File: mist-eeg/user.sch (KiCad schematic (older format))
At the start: 18 parts, among them SW1 START, SW2 USER

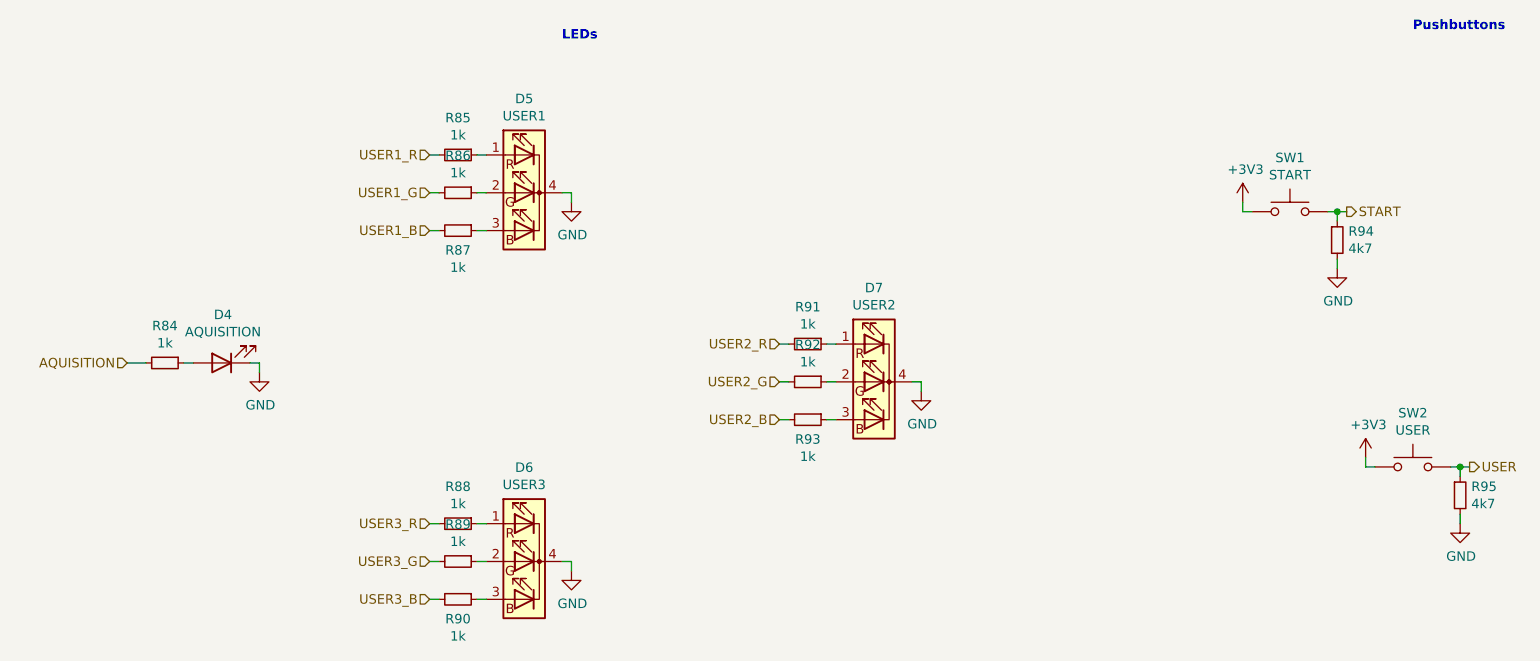
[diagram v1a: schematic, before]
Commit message: Finish schematic and create interface specifications
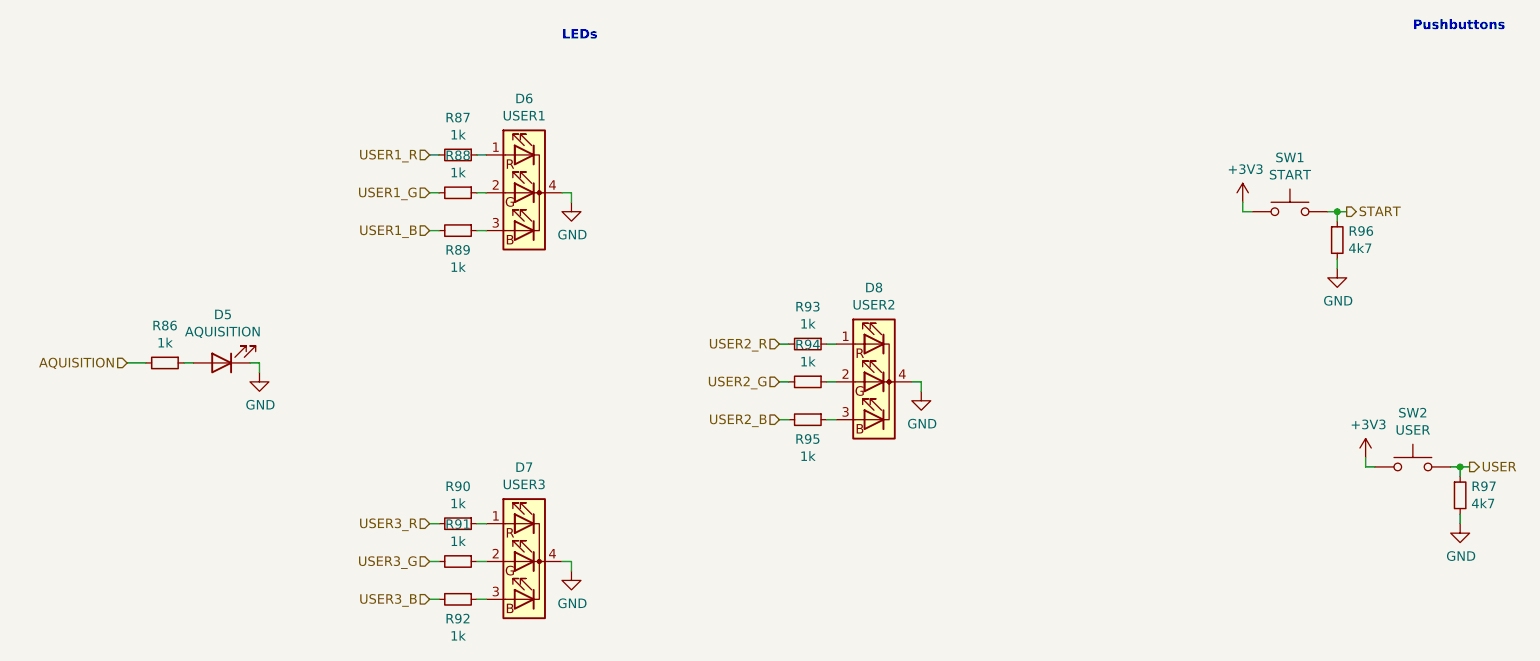
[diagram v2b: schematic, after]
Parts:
- renumbered D4 to D5, D5 to D6, D6 to D7, D7 to D8, R84 to R86, R85 to R87, R86 to R88, R87 to R89, R88 to R90, R89 to R91, R90 to R92, R91 to R93, R92 to R94, R93 to R95, R94 to R96, R95 to R97
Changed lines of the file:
@@
 $EndDescr
 $Comp
-L Device:LED_RGBC D5
+L Device:LED_RGBC D6
 U 1 1 60D2487F
 P 3500 3250
-F 0 "D5" H 3500 3747 50  0000 C CNN
+F 0 "D6" H 3500 3747 50  0000 C CNN
 F 1 "USER1" H 3500 3656 50  0000 C CNN
 F 2 "LED_THT:LED_D5.0mm-4_RGB" H 3500 3200 50  0001 C CNN
@@
 $EndComp
 $Comp
-L power:GND #PWR0108
+L power:GND #PWR0109
 U 1 1 60D255D9
 P 3750 3300
-F 0 "#PWR0108" H 3750 3050 50  0001 C CNN
+F 0 "#PWR0109" H 3750 3050 50  0001 C CNN
 F 1 "GND" H 3755 3127 50  0000 C CNN
 F 2 "" H 3750 3300 50  0001 C CNN
@@
 	3750 3250 3700 3250
 $Comp
-L Device:R_Small R85
+L Device:R_Small R87
 U 1 1 60D26A9C
 P 3150 3050
-F 0 "R85" V 2954 3050 50  0000 C CNN
+F 0 "R87" V 2954 3050 50  0000 C CNN
 F 1 "1k" V 3045 3050 50  0000 C CNN
 F 2 "Resistor_SMD:R_0402_1005Metric" H 3150 3050 50  0001 C CNN
@@
 	3000 3050 3050 3050
 $Comp
-L Device:R_Small R86
+L Device:R_Small R88
 U 1 1 60D27725
 P 3150 3250
-F 0 "R86" V 2954 3250 50  0000 C CNN
+F 0 "R88" V 2954 3250 50  0000 C CNN
 F 1 "1k" V 3045 3250 50  0000 C CNN
 F 2 "Resistor_SMD:R_0402_1005Metric" H 3150 3250 50  0001 C CNN
@@
 	3000 3250 3050 3250
 $Comp
-L Device:R_Small R87
+L Device:R_Small R89
 U 1 1 60D27A38
 P 3150 3450
-F 0 "R87" V 3254 3450 50  0000 C CNN
+F 0 "R89" V 3254 3450 50  0000 C CNN
 F 1 "1k" V 3345 3450 50  0000 C CNN
 F 2 "Resistor_SMD:R_0402_1005Metric" H 3150 3450 50  0001 C CNN
@@
 	3000 3450 3050 3450
 $Comp
-L Device:LED_RGBC D7
+L Device:LED_RGBC D8
 U 1 1 60D29FC0
 P 5350 4250
-F 0 "D7" H 5350 4747 50  0000 C CNN
+F 0 "D8" H 5350 4747 50  0000 C CNN
 F 1 "USER2" H 5350 4656 50  0000 C CNN
 F 2 "LED_THT:LED_D5.0mm-4_RGB" H 5350 4200 50  0001 C CNN
@@
 $EndComp
 $Comp
-L power:GND #PWR0110
+L power:GND #PWR0111
 U 1 1 60D29FC6
 P 5600 4300
-F 0 "#PWR0110" H 5600 4050 50  0001 C CNN
+F 0 "#PWR0111" H 5600 4050 50  0001 C CNN
 F 1 "GND" H 5605 4127 50  0000 C CNN
 F 2 "" H 5600 4300 50  0001 C CNN
@@
 	5600 4250 5550 4250
 $Comp
-L Device:R_Small R91
+L Device:R_Small R93
 U 1 1 60D29FCE
 P 5000 4050
-F 0 "R91" V 4804 4050 50  0000 C CNN
+F 0 "R93" V 4804 4050 50  0000 C CNN
 F 1 "1k" V 4895 4050 50  0000 C CNN
 F 2 "Resistor_SMD:R_0402_1005Metric" H 5000 4050 50  0001 C CNN
@@
 	4850 4050 4900 4050
 $Comp
-L Device:R_Small R92
+L Device:R_Small R94
 U 1 1 60D29FD7
 P 5000 4250
-F 0 "R92" V 4804 4250 50  0000 C CNN
+F 0 "R94" V 4804 4250 50  0000 C CNN
 F 1 "1k" V 4895 4250 50  0000 C CNN
 F 2 "Resistor_SMD:R_0402_1005Metric" H 5000 4250 50  0001 C CNN
@@
 	4850 4250 4900 4250
 $Comp
-L Device:R_Small R93
+L Device:R_Small R95
 U 1 1 60D29FE0
 P 5000 4450
-F 0 "R93" V 5104 4450 50  0000 C CNN
+F 0 "R95" V 5104 4450 50  0000 C CNN
 F 1 "1k" V 5195 4450 50  0000 C CNN
 F 2 "Resistor_SMD:R_0402_1005Metric" H 5000 4450 50  0001 C CNN
@@
 	4850 4450 4900 4450
 $Comp
-L Device:LED_RGBC D6
+L Device:LED_RGBC D7
 U 1 1 60D2CF7B
 P 3500 5200
-F 0 "D6" H 3500 5697 50  0000 C CNN
+F 0 "D7" H 3500 5697 50  0000 C CNN
 F 1 "USER3" H 3500 5606 50  0000 C CNN
 F 2 "LED_THT:LED_D5.0mm-4_RGB" H 3500 5150 50  0001 C CNN
@@
 $EndComp
 $Comp
-L power:GND #PWR0109
+L power:GND #PWR0110
 U 1 1 60D2CF81
 P 3750 5250
-F 0 "#PWR0109" H 3750 5000 50  0001 C CNN
+F 0 "#PWR0110" H 3750 5000 50  0001 C CNN
 F 1 "GND" H 3755 5077 50  0000 C CNN
 F 2 "" H 3750 5250 50  0001 C CNN
@@
 	3750 5200 3700 5200
 $Comp
-L Device:R_Small R88
+L Device:R_Small R90
 U 1 1 60D2CF89
 P 3150 5000
-F 0 "R88" V 2954 5000 50  0000 C CNN
+F 0 "R90" V 2954 5000 50  0000 C CNN
 F 1 "1k" V 3045 5000 50  0000 C CNN
 F 2 "Resistor_SMD:R_0402_1005Metric" H 3150 5000 50  0001 C CNN
@@
 	3000 5000 3050 5000
 $Comp
-L Device:R_Small R89
+L Device:R_Small R91
 U 1 1 60D2CF92
 P 3150 5200
-F 0 "R89" V 2954 5200 50  0000 C CNN
+F 0 "R91" V 2954 5200 50  0000 C CNN
 F 1 "1k" V 3045 5200 50  0000 C CNN
 F 2 "Resistor_SMD:R_0402_1005Metric" H 3150 5200 50  0001 C CNN
@@
 	3000 5200 3050 5200
 $Comp
-L Device:R_Small R90
+L Device:R_Small R92
 U 1 1 60D2CF9B
 P 3150 5400
-F 0 "R90" V 3254 5400 50  0000 C CNN
+F 0 "R92" V 3254 5400 50  0000 C CNN
 F 1 "1k" V 3345 5400 50  0000 C CNN
 F 2 "Resistor_SMD:R_0402_1005Metric" H 3150 5400 50  0001 C CNN
@@
 	7800 3650 7800 3600
 $Comp
-L power:GND #PWR0112
+L power:GND #PWR0113
 U 1 1 60D6D004
 P 7800 3650
-F 0 "#PWR0112" H 7800 3400 50  0001 C CNN
+F 0 "#PWR0113" H 7800 3400 50  0001 C CNN
 F 1 "GND" H 7805 3477 50  0000 C CNN
 F 2 "" H 7800 3650 50  0001 C CNN
@@
 $EndComp
 $Comp
-L Device:R_Small R94
+L Device:R_Small R96
 U 1 1 60D6CBEB
 P 7800 3500
-F 0 "R94" H 7859 3546 50  0000 L CNN
+F 0 "R96" H 7859 3546 50  0000 L CNN
 F 1 "4k7" H 7859 3455 50  0000 L CNN
 F 2 "Resistor_SMD:R_0201_0603Metric" H 7800 3500 50  0001 C CNN
@@
 	2100 4200 2100 4150
 $Comp
-L power:GND #PWR0107
+L power:GND #PWR0108
 U 1 1 60D1F73E
 P 2100 4200
-F 0 "#PWR0107" H 2100 3950 50  0001 C CNN
+F 0 "#PWR0108" H 2100 3950 50  0001 C CNN
 F 1 "GND" H 2105 4027 50  0000 C CNN
 F 2 "" H 2100 4200 50  0001 C CNN
@@
 	1700 4150 1750 4150
 $Comp
-L Device:R_Small R84
+L Device:R_Small R86
 U 1 1 60D1C4D3
 P 1600 4150
-F 0 "R84" V 1404 4150 50  0000 C CNN
+F 0 "R86" V 1404 4150 50  0000 C CNN
 F 1 "1k" V 1495 4150 50  0000 C CNN
 F 2 "Resistor_SMD:R_0402_1005Metric" H 1600 4150 50  0001 C CNN
@@
 $EndComp
 $Comp
-L Device:LED D4
+L Device:LED D5
 U 1 1 60D180B3
 P 1900 4150
-F 0 "D4" H 1893 3895 50  0000 C CNN
+F 0 "D5" H 1893 3895 50  0000 C CNN
 F 1 "AQUISITION" H 1893 3986 50  0000 C CNN
 F 2 "LED_THT:LED_D3.0mm" H 1900 4150 50  0001 C CNN
@@
 $EndComp
 $Comp
-L power:+3V3 #PWR0111
+L power:+3V3 #PWR0112
 U 1 1 61146B19
 P 7300 3300
-F 0 "#PWR0111" H 7300 3150 50  0001 C CNN
+F 0 "#PWR0112" H 7300 3150 50  0001 C CNN
 F 1 "+3V3" H 7315 3473 50  0000 C CNN
 F 2 "" H 7300 3300 50  0001 C CNN
@@
 	8450 5000 8450 4950
 $Comp
-L power:GND #PWR0114
+L power:GND #PWR0115
 U 1 1 61304D1F
 P 8450 5000
-F 0 "#PWR0114" H 8450 4750 50  0001 C CNN
+F 0 "#PWR0115" H 8450 4750 50  0001 C CNN
 F 1 "GND" H 8455 4827 50  0000 C CNN
 F 2 "" H 8450 5000 50  0001 C CNN
@@
 $EndComp
 $Comp
-L Device:R_Small R95
+L Device:R_Small R97
 U 1 1 61304D25
 P 8450 4850
-F 0 "R95" H 8509 4896 50  0000 L CNN
+F 0 "R97" H 8509 4896 50  0000 L CNN
 F 1 "4k7" H 8509 4805 50  0000 L CNN
 F 2 "Resistor_SMD:R_0201_0603Metric" H 8450 4850 50  0001 C CNN
@@
 $EndComp
 $Comp
-L power:+3V3 #PWR0113
+L power:+3V3 #PWR0114
 U 1 1 61304D31
 P 7950 4650
-F 0 "#PWR0113" H 7950 4500 50  0001 C CNN
+F 0 "#PWR0114" H 7950 4500 50  0001 C CNN
 F 1 "+3V3" H 7965 4823 50  0000 C CNN
 F 2 "" H 7950 4650 50  0001 C CNN

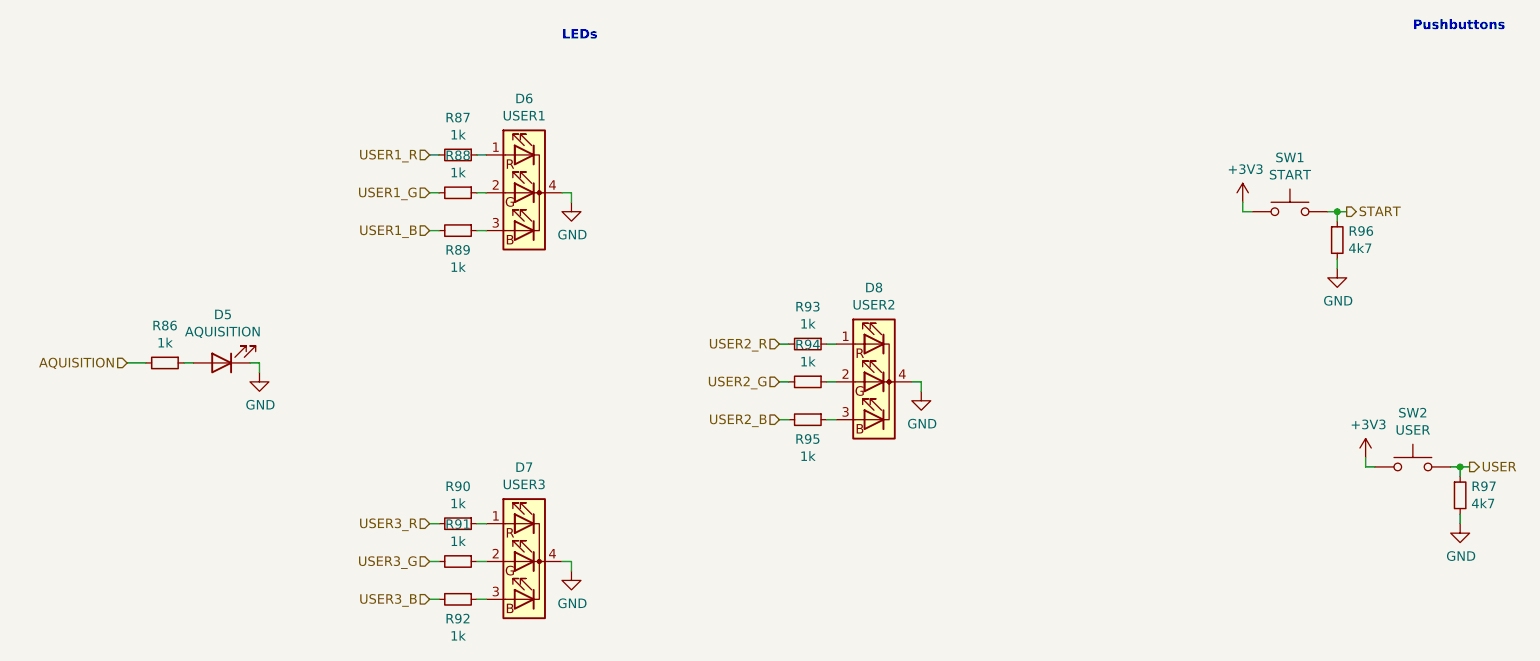
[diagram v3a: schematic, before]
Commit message: Change buckboost regulator used
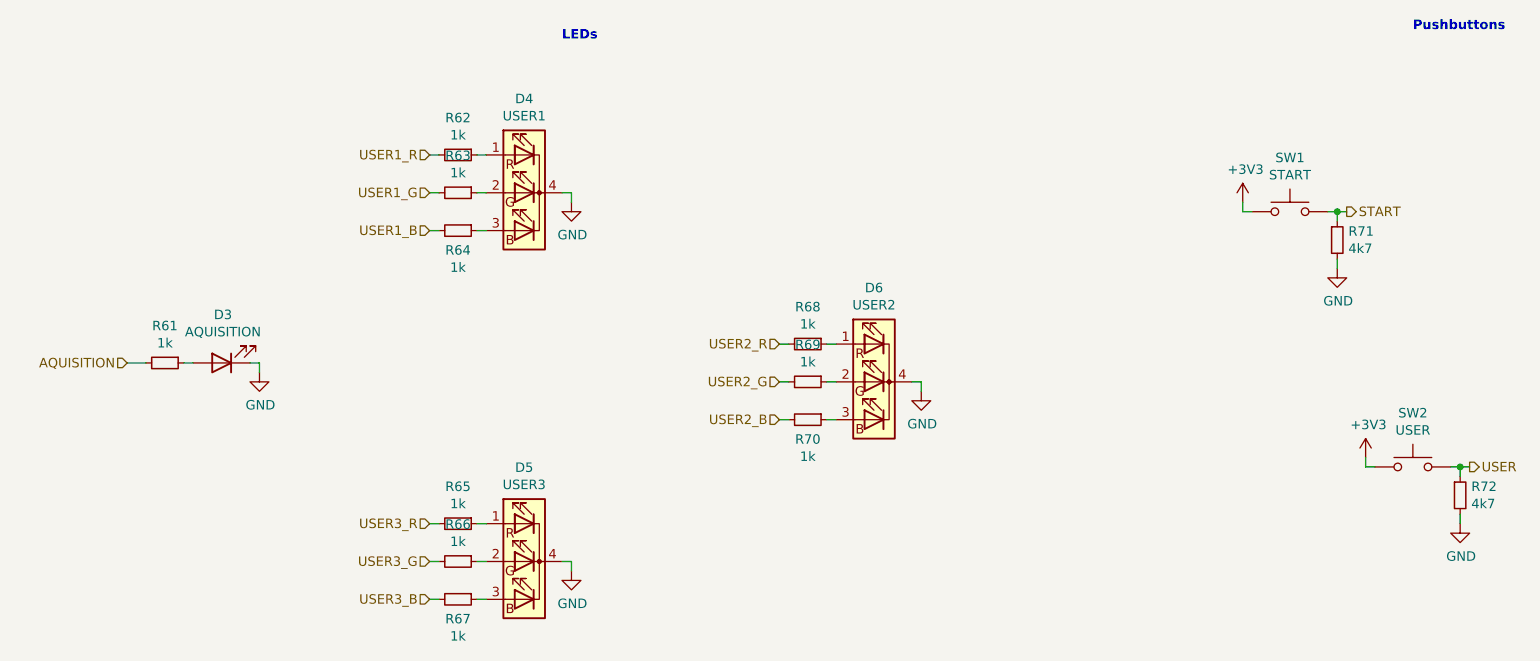
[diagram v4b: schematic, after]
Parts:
- renumbered D5 to D3, D6 to D4, D7 to D5, D8 to D6, R86 to R61, R87 to R62, R88 to R63, R89 to R64, R90 to R65, R91 to R66, R92 to R67, R93 to R68, R94 to R69, R95 to R70, R96 to R71, R97 to R72
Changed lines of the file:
@@
 Sheet 9 11
 Title "Portiloop"
-Date "2021-06-07"
-Rev "1A"
+Date "2021-08-03"
+Rev "1D"
 Comp "MIST Lab"
 Comment1 "Designed by Xavier L'Heureux"
@@
 $EndDescr
 $Comp
-L Device:LED_RGBC D6
+L Device:LED_RGBC D4
 U 1 1 60D2487F
 P 3500 3250
-F 0 "D6" H 3500 3747 50  0000 C CNN
+F 0 "D4" H 3500 3747 50  0000 C CNN
 F 1 "USER1" H 3500 3656 50  0000 C CNN
 F 2 "LED_THT:LED_D5.0mm-4_RGB" H 3500 3200 50  0001 C CNN
@@
 $EndComp
 $Comp
-L power:GND #PWR0109
+L power:GND #PWR088
 U 1 1 60D255D9
 P 3750 3300
-F 0 "#PWR0109" H 3750 3050 50  0001 C CNN
+F 0 "#PWR088" H 3750 3050 50  0001 C CNN
 F 1 "GND" H 3755 3127 50  0000 C CNN
 F 2 "" H 3750 3300 50  0001 C CNN
@@
 	3750 3250 3700 3250
 $Comp
-L Device:R_Small R87
+L Device:R_Small R62
 U 1 1 60D26A9C
 P 3150 3050
-F 0 "R87" V 2954 3050 50  0000 C CNN
+F 0 "R62" V 2954 3050 50  0000 C CNN
 F 1 "1k" V 3045 3050 50  0000 C CNN
 F 2 "Resistor_SMD:R_0402_1005Metric" H 3150 3050 50  0001 C CNN
@@
 	3000 3050 3050 3050
 $Comp
-L Device:R_Small R88
+L Device:R_Small R63
 U 1 1 60D27725
 P 3150 3250
-F 0 "R88" V 2954 3250 50  0000 C CNN
+F 0 "R63" V 2954 3250 50  0000 C CNN
 F 1 "1k" V 3045 3250 50  0000 C CNN
 F 2 "Resistor_SMD:R_0402_1005Metric" H 3150 3250 50  0001 C CNN
@@
 	3000 3250 3050 3250
 $Comp
-L Device:R_Small R89
+L Device:R_Small R64
 U 1 1 60D27A38
 P 3150 3450
-F 0 "R89" V 3254 3450 50  0000 C CNN
+F 0 "R64" V 3254 3450 50  0000 C CNN
 F 1 "1k" V 3345 3450 50  0000 C CNN
 F 2 "Resistor_SMD:R_0402_1005Metric" H 3150 3450 50  0001 C CNN
@@
 	3000 3450 3050 3450
 $Comp
-L Device:LED_RGBC D8
+L Device:LED_RGBC D6
 U 1 1 60D29FC0
 P 5350 4250
-F 0 "D8" H 5350 4747 50  0000 C CNN
+F 0 "D6" H 5350 4747 50  0000 C CNN
 F 1 "USER2" H 5350 4656 50  0000 C CNN
 F 2 "LED_THT:LED_D5.0mm-4_RGB" H 5350 4200 50  0001 C CNN
@@
 $EndComp
 $Comp
-L power:GND #PWR0111
+L power:GND #PWR090
 U 1 1 60D29FC6
 P 5600 4300
-F 0 "#PWR0111" H 5600 4050 50  0001 C CNN
+F 0 "#PWR090" H 5600 4050 50  0001 C CNN
 F 1 "GND" H 5605 4127 50  0000 C CNN
 F 2 "" H 5600 4300 50  0001 C CNN
@@
 	5600 4250 5550 4250
 $Comp
-L Device:R_Small R93
+L Device:R_Small R68
 U 1 1 60D29FCE
 P 5000 4050
-F 0 "R93" V 4804 4050 50  0000 C CNN
+F 0 "R68" V 4804 4050 50  0000 C CNN
 F 1 "1k" V 4895 4050 50  0000 C CNN
 F 2 "Resistor_SMD:R_0402_1005Metric" H 5000 4050 50  0001 C CNN
@@
 	4850 4050 4900 4050
 $Comp
-L Device:R_Small R94
+L Device:R_Small R69
 U 1 1 60D29FD7
 P 5000 4250
-F 0 "R94" V 4804 4250 50  0000 C CNN
+F 0 "R69" V 4804 4250 50  0000 C CNN
 F 1 "1k" V 4895 4250 50  0000 C CNN
 F 2 "Resistor_SMD:R_0402_1005Metric" H 5000 4250 50  0001 C CNN
@@
 	4850 4250 4900 4250
 $Comp
-L Device:R_Small R95
+L Device:R_Small R70
 U 1 1 60D29FE0
 P 5000 4450
-F 0 "R95" V 5104 4450 50  0000 C CNN
+F 0 "R70" V 5104 4450 50  0000 C CNN
 F 1 "1k" V 5195 4450 50  0000 C CNN
 F 2 "Resistor_SMD:R_0402_1005Metric" H 5000 4450 50  0001 C CNN
@@
 	4850 4450 4900 4450
 $Comp
-L Device:LED_RGBC D7
+L Device:LED_RGBC D5
 U 1 1 60D2CF7B
 P 3500 5200
-F 0 "D7" H 3500 5697 50  0000 C CNN
+F 0 "D5" H 3500 5697 50  0000 C CNN
 F 1 "USER3" H 3500 5606 50  0000 C CNN
 F 2 "LED_THT:LED_D5.0mm-4_RGB" H 3500 5150 50  0001 C CNN
@@
 $EndComp
 $Comp
-L power:GND #PWR0110
+L power:GND #PWR089
 U 1 1 60D2CF81
 P 3750 5250
-F 0 "#PWR0110" H 3750 5000 50  0001 C CNN
+F 0 "#PWR089" H 3750 5000 50  0001 C CNN
 F 1 "GND" H 3755 5077 50  0000 C CNN
 F 2 "" H 3750 5250 50  0001 C CNN
@@
 	3750 5200 3700 5200
 $Comp
-L Device:R_Small R90
+L Device:R_Small R65
 U 1 1 60D2CF89
 P 3150 5000
-F 0 "R90" V 2954 5000 50  0000 C CNN
+F 0 "R65" V 2954 5000 50  0000 C CNN
 F 1 "1k" V 3045 5000 50  0000 C CNN
 F 2 "Resistor_SMD:R_0402_1005Metric" H 3150 5000 50  0001 C CNN
@@
 	3000 5000 3050 5000
 $Comp
-L Device:R_Small R91
+L Device:R_Small R66
 U 1 1 60D2CF92
 P 3150 5200
-F 0 "R91" V 2954 5200 50  0000 C CNN
+F 0 "R66" V 2954 5200 50  0000 C CNN
 F 1 "1k" V 3045 5200 50  0000 C CNN
 F 2 "Resistor_SMD:R_0402_1005Metric" H 3150 5200 50  0001 C CNN
@@
 	3000 5200 3050 5200
 $Comp
-L Device:R_Small R92
+L Device:R_Small R67
 U 1 1 60D2CF9B
 P 3150 5400
-F 0 "R92" V 3254 5400 50  0000 C CNN
+F 0 "R67" V 3254 5400 50  0000 C CNN
 F 1 "1k" V 3345 5400 50  0000 C CNN
 F 2 "Resistor_SMD:R_0402_1005Metric" H 3150 5400 50  0001 C CNN
@@
 	7800 3650 7800 3600
 $Comp
-L power:GND #PWR0113
+L power:GND #PWR092
 U 1 1 60D6D004
 P 7800 3650
-F 0 "#PWR0113" H 7800 3400 50  0001 C CNN
+F 0 "#PWR092" H 7800 3400 50  0001 C CNN
 F 1 "GND" H 7805 3477 50  0000 C CNN
 F 2 "" H 7800 3650 50  0001 C CNN
@@
 $EndComp
 $Comp
-L Device:R_Small R96
+L Device:R_Small R71
 U 1 1 60D6CBEB
 P 7800 3500
-F 0 "R96" H 7859 3546 50  0000 L CNN
+F 0 "R71" H 7859 3546 50  0000 L CNN
 F 1 "4k7" H 7859 3455 50  0000 L CNN
 F 2 "Resistor_SMD:R_0201_0603Metric" H 7800 3500 50  0001 C CNN
@@
 	2100 4200 2100 4150
 $Comp
-L power:GND #PWR0108
+L power:GND #PWR087
 U 1 1 60D1F73E
 P 2100 4200
-F 0 "#PWR0108" H 2100 3950 50  0001 C CNN
+F 0 "#PWR087" H 2100 3950 50  0001 C CNN
 F 1 "GND" H 2105 4027 50  0000 C CNN
 F 2 "" H 2100 4200 50  0001 C CNN
@@
 	1700 4150 1750 4150
 $Comp
-L Device:R_Small R86
+L Device:R_Small R61
 U 1 1 60D1C4D3
 P 1600 4150
-F 0 "R86" V 1404 4150 50  0000 C CNN
+F 0 "R61" V 1404 4150 50  0000 C CNN
 F 1 "1k" V 1495 4150 50  0000 C CNN
 F 2 "Resistor_SMD:R_0402_1005Metric" H 1600 4150 50  0001 C CNN
@@
 $EndComp
 $Comp
-L Device:LED D5
+L Device:LED D3
 U 1 1 60D180B3
 P 1900 4150
-F 0 "D5" H 1893 3895 50  0000 C CNN
+F 0 "D3" H 1893 3895 50  0000 C CNN
 F 1 "AQUISITION" H 1893 3986 50  0000 C CNN
 F 2 "LED_THT:LED_D3.0mm" H 1900 4150 50  0001 C CNN
@@
 $EndComp
 $Comp
-L power:+3V3 #PWR0112
+L power:+3V3 #PWR091
 U 1 1 61146B19
 P 7300 3300
-F 0 "#PWR0112" H 7300 3150 50  0001 C CNN
+F 0 "#PWR091" H 7300 3150 50  0001 C CNN
 F 1 "+3V3" H 7315 3473 50  0000 C CNN
 F 2 "" H 7300 3300 50  0001 C CNN
@@
 	8450 5000 8450 4950
 $Comp
-L power:GND #PWR0115
+L power:GND #PWR094
 U 1 1 61304D1F
 P 8450 5000
-F 0 "#PWR0115" H 8450 4750 50  0001 C CNN
+F 0 "#PWR094" H 8450 4750 50  0001 C CNN
 F 1 "GND" H 8455 4827 50  0000 C CNN
 F 2 "" H 8450 5000 50  0001 C CNN
@@
 $EndComp
 $Comp
-L Device:R_Small R97
+L Device:R_Small R72
 U 1 1 61304D25
 P 8450 4850
-F 0 "R97" H 8509 4896 50  0000 L CNN
+F 0 "R72" H 8509 4896 50  0000 L CNN
 F 1 "4k7" H 8509 4805 50  0000 L CNN
 F 2 "Resistor_SMD:R_0201_0603Metric" H 8450 4850 50  0001 C CNN
@@
 $EndComp
 $Comp
-L power:+3V3 #PWR0114
+L power:+3V3 #PWR093
 U 1 1 61304D31
 P 7950 4650
-F 0 "#PWR0114" H 7950 4500 50  0001 C CNN
+F 0 "#PWR093" H 7950 4500 50  0001 C CNN
 F 1 "+3V3" H 7965 4823 50  0000 C CNN
 F 2 "" H 7950 4650 50  0001 C CNN
